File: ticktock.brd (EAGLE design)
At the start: 61 x 67.3 mm, 66 parts, among them IC1 ATMEGA644A, IC2 AD8611RM, IC3 REF200U, J1 AVR_SPI_PRG_6NS, Q1 MOSFET-NCHANNEL2N7002PW, Q2 MOSFET-NCHANNELBSS138, Q3 MOSFET-NCHANNELBSS138, U1 MAX232SOIC16, U2 OSCILLATORSMD, U3 FT232RLSSOP, U4 BMP180, X2 DB9 Male

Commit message: Relabel USB_TX and USB_RX to be consistent with MCU's perspective
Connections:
- net USB_RX: now also IC1.9, U3.1; no longer IC1.10, U3.5
- net USB_TX: now also IC1.10, U3.5; no longer IC1.9, U3.1
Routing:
- net USB_TX: track 27.5 -> 17.5 mm
- net USB_RX: track 17.5 -> 27.5 mm
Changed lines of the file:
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@@
 <wire x1="42.418" y1="8.108" x2="43.2" y2="8.89" width="0.381" layer="16"/>
 </signal>
-<signal name="USB_RX">
+<signal name="USB_TX">
 <contactref element="IC1" pad="10"/>
 <via x="30.734" y="6.858" extent="1-16" drill="0.6"/>
@@
 <wire x1="32.105" y1="7.721" x2="32.105" y2="8.736" width="0.4064" layer="1"/>
 </signal>
-<signal name="USB_TX">
+<signal name="USB_RX">
 <contactref element="IC1" pad="9"/>
 <via x="30.734" y="4.572" extent="1-16" drill="0.6"/>

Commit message: Reroute right angle wire
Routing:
- net MOSI: track 9.90 -> 11.0 mm
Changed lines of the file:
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@@
 <wire x1="30.48" y1="35.56" x2="31.242" y2="35.56" width="0.508" layer="1"/>
 <wire x1="31.242" y1="35.56" x2="32.258" y2="34.544" width="0.508" layer="1"/>
-<wire x1="32.258" y1="34.544" x2="32.258" y2="26.902" width="0.508" layer="1"/>
 <wire x1="32.258" y1="26.902" x2="32.3" y2="26.86" width="0.508" layer="1"/>
+<wire x1="32.258" y1="26.902" x2="31.772" y2="26.902" width="0.508" layer="1"/>
+<wire x1="31.772" y1="26.902" x2="31.242" y2="27.432" width="0.508" layer="1"/>
+<wire x1="31.242" y1="27.432" x2="31.242" y2="27.94" width="0.508" layer="1"/>
+<wire x1="31.242" y1="27.94" x2="32.258" y2="28.956" width="0.508" layer="1"/>
+<wire x1="32.258" y1="28.956" x2="32.258" y2="34.544" width="0.508" layer="1"/>
 </signal>
 <signal name="SCK">

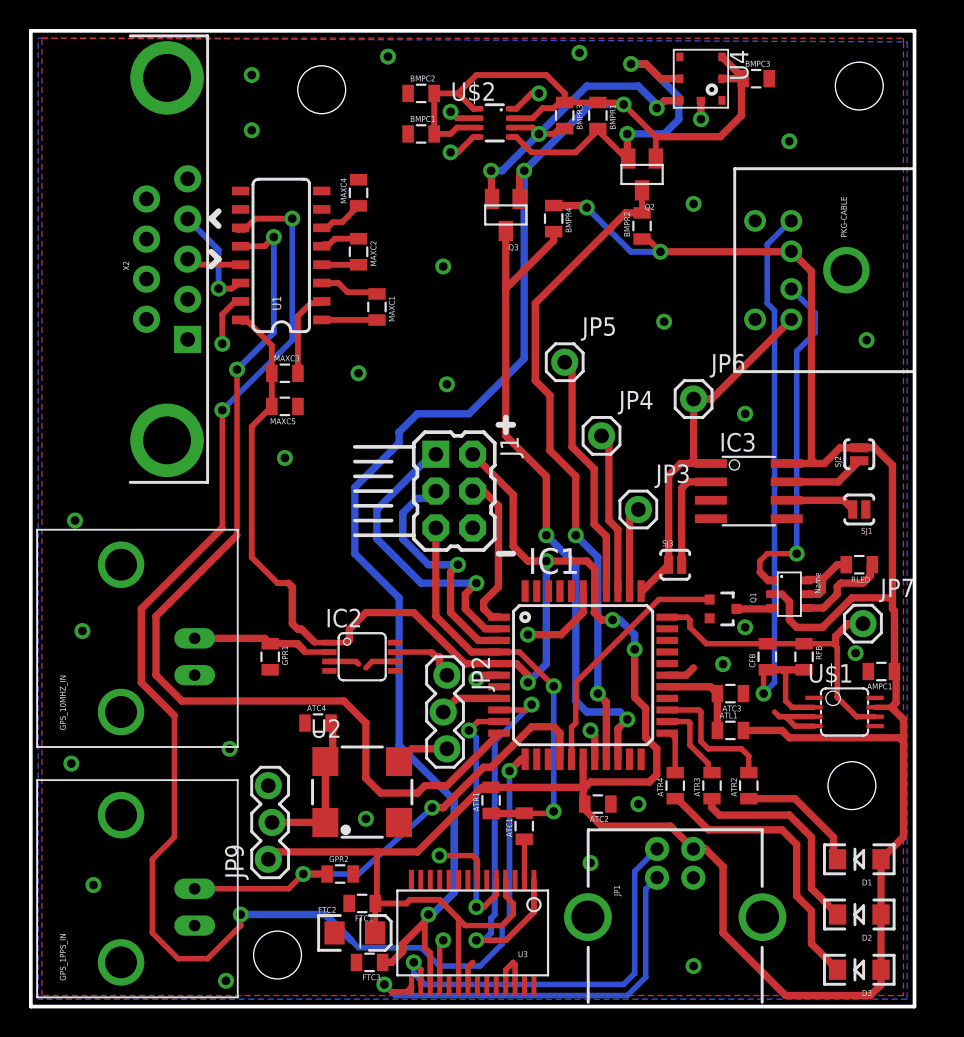
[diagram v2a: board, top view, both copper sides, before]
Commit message: Add silkscreen for MAX232
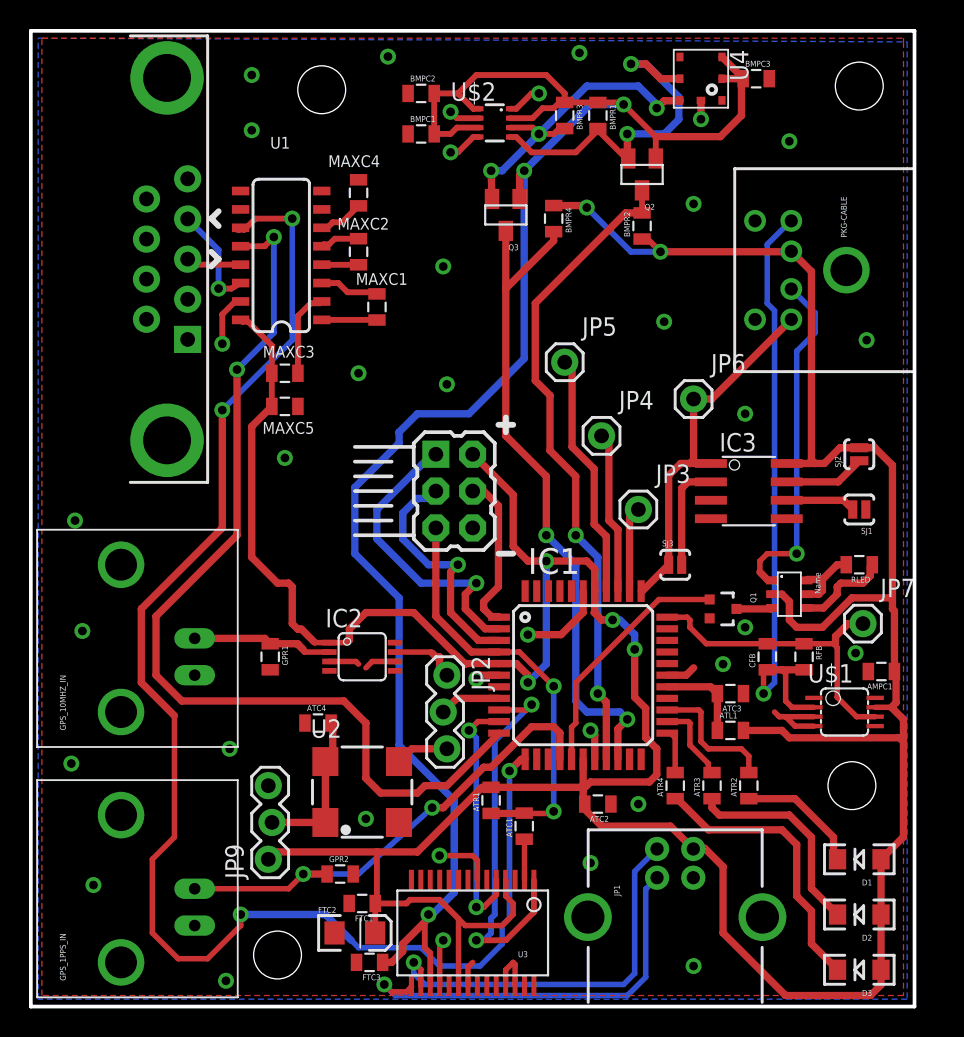
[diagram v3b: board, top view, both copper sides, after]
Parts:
- J1: value AVR_SPI_PRG_6NS -> ISP PGMR
- U1: value MAX232SOIC16 -> MAX232

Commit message: Start working on silkscreen
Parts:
- D1: value RED -> ERR
- D2: value Yellow -> ACT
- D3: value GREEN -> SEND
- GPS10MHZ, GPS1PPS: value BNCPTH -> BNC Conn
- IC2: value AD8611RM -> AD8611
- JP1: value USB-B -> Square USB
- U$2: value BME280BME280-LGA -> BME280
- U2: value OSCILLATORSMD -> 10MHz XTAL
- U3: value FT232RLSSOP -> FT232
- renumbered GPS_10MHZ_IN to GPS10MHZ, GPS_1PPS_IN to GPS1PPS
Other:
- board text added: "FTDI"
- board text added: "GPS"
- board text added: "MCU"
- board text added: "RS232"
- board text added: "SENSOR BLOCK"

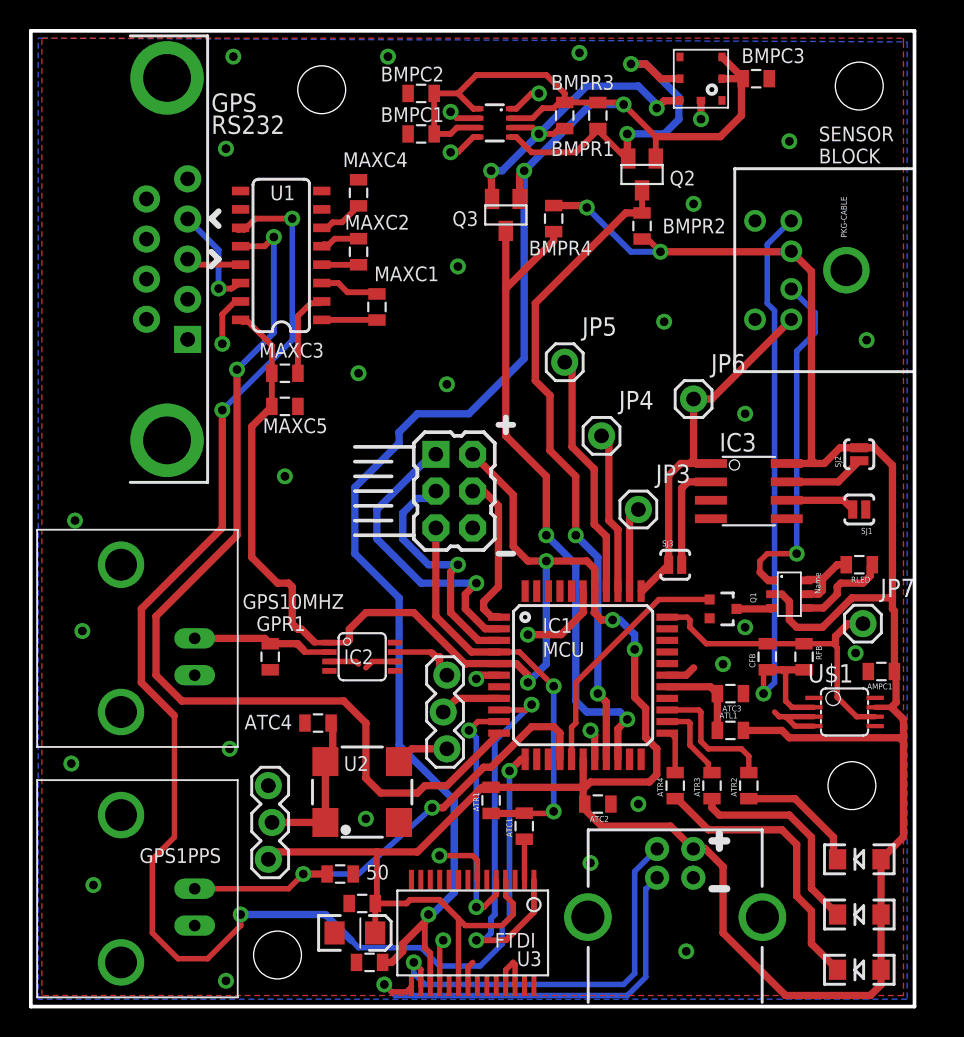
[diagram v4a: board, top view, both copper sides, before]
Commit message: Finish preliminary silkscreen
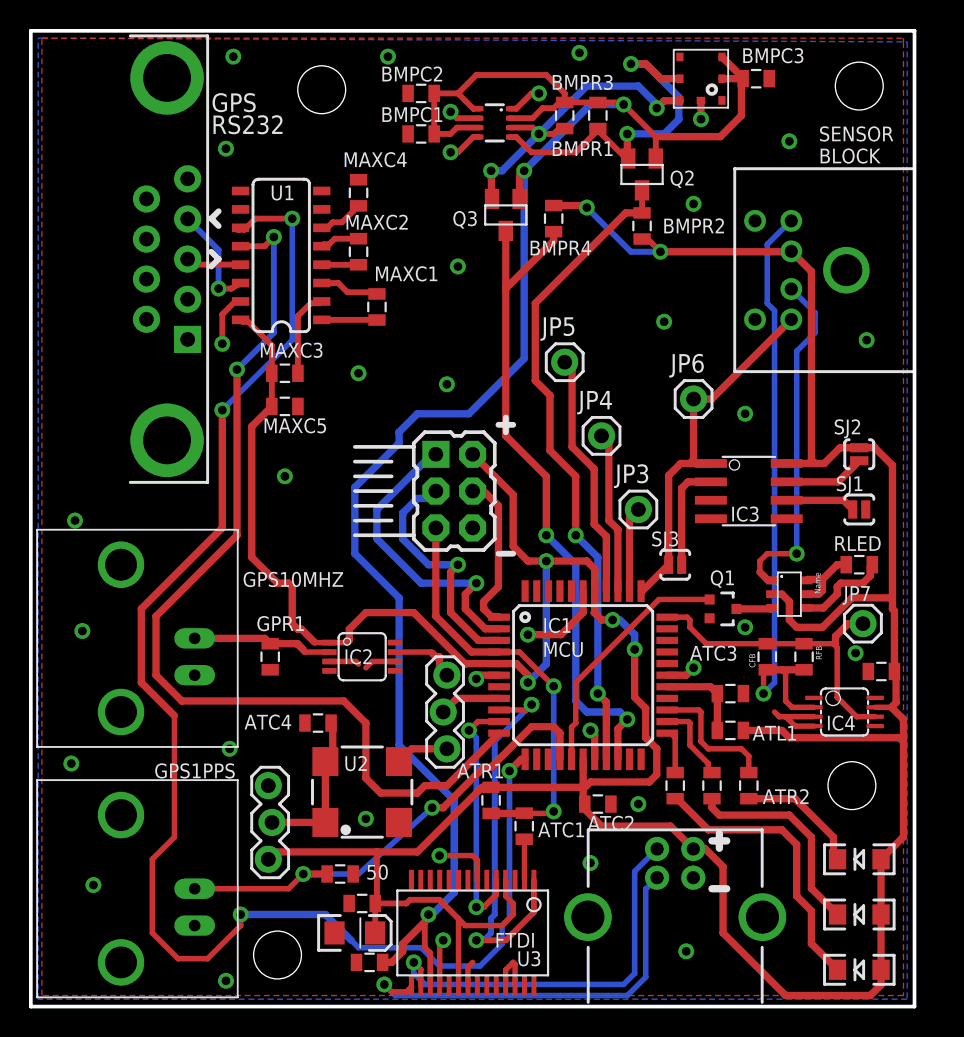
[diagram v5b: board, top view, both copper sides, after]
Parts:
- ATC1, ATC2: value 0.1uF -> .1uF
- IC3: value REF200U -> REF200
- PKG-CABLE: value MINI-DIN6PTH -> MINI DIN-6
- renumbered U$1 to IC4

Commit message: More work on silkscreen
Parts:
- U2: value 10MHz XTAL -> XTAL
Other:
- board text added: "CLK SEL"
- board text added: "PWR XTAL"
- board text added: "XTAL"
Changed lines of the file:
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@@
 <layer number="18" name="Vias" color="2" fill="1" visible="no" active="yes"/>
 <layer number="19" name="Unrouted" color="6" fill="1" visible="no" active="yes"/>
-<layer number="20" name="Dimension" color="15" fill="1" visible="no" active="yes"/>
-<layer number="21" name="tPlace" color="7" fill="1" visible="yes" active="yes"/>
+<layer number="20" name="Dimension" color="15" fill="1" visible="yes" active="yes"/>
+<layer number="21" name="tPlace" color="7" fill="1" visible="no" active="yes"/>
 <layer number="22" name="bPlace" color="7" fill="1" visible="no" active="yes"/>
-<layer number="23" name="tOrigins" color="15" fill="1" visible="yes" active="yes"/>
+<layer number="23" name="tOrigins" color="15" fill="1" visible="no" active="yes"/>
 <layer number="24" name="bOrigins" color="15" fill="1" visible="no" active="yes"/>
 <layer number="25" name="tNames" color="7" fill="1" visible="yes" active="yes"/>
@@
 <text x="54.356" y="58.166" size="1.016" layer="25" ratio="20">SENSOR
 BLOCK</text>
+<wire x1="18.288" y1="13.208" x2="18.288" y2="9.652" width="0.254" layer="25"/>
+<text x="19.05" y="9.652" size="0.508" layer="25" ratio="20" rot="R90">PWR XTAL</text>
+<wire x1="26.924" y1="20.828" x2="26.924" y2="17.272" width="0.254" layer="25"/>
+<wire x1="30.226" y1="19.812" x2="30.226" y2="23.368" width="0.254" layer="25"/>
+<text x="26.416" y="18.542" size="0.508" layer="25" ratio="20" rot="R90">XTAL</text>
+<text x="30.988" y="20.574" size="0.508" layer="25" ratio="20" rot="R90">GPS</text>
+<text x="27.178" y="24.892" size="1.016" layer="25" ratio="20">CLK
+SEL</text>
 </plain>
 <attributes>
@@
 </element>
 <element name="MAXC1" library="SparkFun-Capacitors" package="0805" value="1uF" x="23.876" y="48.26" smashed="yes" rot="R270">
-<attribute name="NAME" x="23.6855" y="50.038" size="1.016" layer="25" ratio="20"/>
 <attribute name="VALUE" x="25.019" y="48.768" size="1.016" layer="27" ratio="20"/>
 </element>
 <element name="MAXC2" library="SparkFun-Capacitors" package="0805" value="1uF" x="22.606" y="52.07" smashed="yes" rot="R270">
-<attribute name="NAME" x="21.6535" y="53.594" size="1.016" layer="25" ratio="20"/>
 <attribute name="VALUE" x="23.749" y="52.324" size="1.016" layer="27" ratio="20"/>
 </element>
@@
 </element>
 <element name="MAXC3" library="SparkFun-Capacitors" package="0805" value="1uF" x="17.526" y="43.688" smashed="yes">
-<attribute name="NAME" x="15.748" y="44.7675" size="1.016" layer="25" ratio="20"/>
 <attribute name="VALUE" x="19.304" y="43.561" size="1.016" layer="27" ratio="20"/>
 </element>
 <element name="MAXC5" library="SparkFun-Capacitors" package="0805" value="1uF" x="17.526" y="41.402" smashed="yes" rot="R180">
-<attribute name="NAME" x="16.002" y="39.5605" size="1.016" layer="25" ratio="20"/>
-<attribute name="VALUE" x="16.764" y="38.227" size="1.016" layer="27" ratio="20"/>
+<attribute name="VALUE" x="19.304" y="40.767" size="1.016" layer="27" ratio="20"/>
 </element>
 <element name="MAXC4" library="SparkFun-Capacitors" package="0805" value="1uF" x="22.606" y="56.134" smashed="yes" rot="R90">
-<attribute name="NAME" x="21.5265" y="57.912" size="1.016" layer="25" ratio="20"/>
 <attribute name="VALUE" x="23.749" y="56.642" size="1.016" layer="27" ratio="20"/>
 </element>
@@
 <attribute name="OC_FARNELL" value="1455123" x="38.1" y="22.86" size="1.778" layer="27" display="off"/>
 <attribute name="NAME" x="35.306" y="25.781" size="1.016" layer="25" ratio="20"/>
-<attribute name="VALUE" x="33.655" y="15.1209" size="1.016" layer="27" ratio="20"/>
 </element>
 <element name="U3" library="SparkFun-DigitalIC" package="SSOP28DB" value="FT232" x="30.48" y="5.08" smashed="yes" rot="R180">
@@
 </element>
 <element name="FTC1" library="SparkFun-Capacitors" package="0805" value="0.1uF" x="22.86" y="7.112" smashed="yes" rot="R180">
-<attribute name="VALUE" x="17.272" y="6.985" size="1.016" layer="27" ratio="20"/>
+<attribute name="VALUE" x="17.272" y="6.731" size="1.016" layer="27" ratio="20"/>
 </element>
 <element name="FTC3" library="SparkFun-Capacitors" package="0805" value="0.1uF" x="23.368" y="3.048" smashed="yes" rot="R180">
@@
 </element>
 <element name="ATC1" library="SparkFun-Capacitors" package="0805" value=".1uF" x="34.036" y="12.446" smashed="yes" rot="R90">
-<attribute name="NAME" x="34.9885" y="11.684" size="1.016" layer="25" ratio="20"/>
-<attribute name="VALUE" x="34.925" y="10.414" size="1.016" layer="27" ratio="20"/>
+<attribute name="VALUE" x="34.925" y="11.176" size="1.016" layer="27" ratio="20"/>
 </element>
 <element name="FTC2" library="SparkFun-Capacitors" package="EIA3216" value="10uF" x="22.352" y="5.08" smashed="yes">
-<attribute name="VALUE" x="16.156" y="5.65" size="1.016" layer="27" ratio="20"/>
+<attribute name="VALUE" x="16.156" y="5.396" size="1.016" layer="27" ratio="20"/>
 </element>
 <element name="ATR1" library="SparkFun-Resistors" package="0805" value="10K" x="31.75" y="14.224" smashed="yes" rot="R90">
-<attribute name="NAME" x="29.4005" y="15.748" size="1.016" layer="25" ratio="20"/>
 <attribute name="VALUE" x="28.321" y="14.478" size="1.016" layer="27" ratio="20"/>
 </element>
 <element name="ATC2" library="SparkFun-Capacitors" package="0805" value=".1uF" x="39.116" y="13.97" smashed="yes" rot="R180">
-<attribute name="NAME" x="38.4048" y="12.1285" size="1.016" layer="25" ratio="20"/>
 <attribute name="VALUE" x="40.64" y="13.843" size="1.016" layer="27" ratio="20"/>
 </element>
 <element name="ATL1" library="SparkFun-Passives" package="0805" value="10uH" x="48.26" y="19.05" smashed="yes">
-<attribute name="NAME" x="49.784" y="18.3515" size="1.016" layer="25" ratio="20"/>
-<attribute name="VALUE" x="49.022" y="17.145" size="1.016" layer="27" ratio="20"/>
+<attribute name="VALUE" x="49.53" y="17.399" size="1.016" layer="27" ratio="20"/>
 </element>
 <element name="ATC3" library="SparkFun-Capacitors" package="0805" value="0.1uF" x="48.26" y="21.59" smashed="yes" rot="R180">
-<attribute name="NAME" x="45.466" y="23.8633" size="1.016" layer="25" ratio="20"/>
 <attribute name="VALUE" x="45.466" y="22.733" size="1.016" layer="27" ratio="20"/>
 </element>
@@
 <attribute name="VALUE" x="22.987" y="40.132" size="1.016" layer="27" ratio="20"/>
 </element>
-<element name="U2" library="SparkFun-FreqCtrl" package="CRYSTAL-SMD-7X5" value="10MHz XTAL" x="20.32" y="12.7" smashed="yes">
+<element name="U2" library="SparkFun-FreqCtrl" package="CRYSTAL-SMD-7X5" value="XTAL" x="20.32" y="12.7" smashed="yes">
 <attribute name="NAME" x="21.59" y="16.256" size="1.016" layer="25" ratio="20"/>
-<attribute name="VALUE" x="18.288" y="10.287" size="1.016" layer="27" ratio="20"/>
+<attribute name="VALUE" x="23.368" y="10.287" size="1.016" layer="27" ratio="20"/>
 </element>
 <element name="ATC4" library="SparkFun-Capacitors" package="0805" value="0.01uF" x="19.812" y="19.558" smashed="yes">
@@
 </element>
 <element name="GPR1" library="SparkFun-Resistors" package="0805" value="50" x="16.51" y="24.13" smashed="yes" rot="R270">
-<attribute name="NAME" x="15.5575" y="25.908" size="1.016" layer="25" ratio="20"/>
-<attribute name="VALUE" x="17.399" y="24.638" size="1.016" layer="27" ratio="20"/>
+<attribute name="VALUE" x="15.621" y="25.908" size="1.016" layer="27" ratio="20"/>
 </element>
 <element name="GPR2" library="SparkFun-Resistors" package="0805" value="50" x="21.336" y="9.144" smashed="yes">
-<attribute name="VALUE" x="23.114" y="8.763" size="1.016" layer="25" ratio="20"/>
+<attribute name="VALUE" x="22.86" y="8.763" size="1.016" layer="25" ratio="20"/>
 </element>
 <element name="RFB" library="SparkFun-Resistors" package="0805" value="1K" x="53.34" y="24.13" smashed="yes" rot="R270">
@@
 </element>
 <element name="BMPR1" library="SparkFun-Resistors" package="0805" value="10K" x="39.116" y="61.468" smashed="yes" rot="R270">
-<attribute name="NAME" x="35.8775" y="58.674" size="1.016" layer="25" ratio="20"/>
+<attribute name="VALUE" x="37.211" y="58.674" size="1.016" layer="27" ratio="20"/>
 </element>
 <element name="BMPR2" library="SparkFun-Resistors" package="0805" value="10K" x="42.164" y="53.848" smashed="yes" rot="R90">
@@
 </element>
 <element name="BMPR3" library="SparkFun-Resistors" package="0805" value="10K" x="36.83" y="61.468" smashed="yes" rot="R270">
-<attribute name="NAME" x="35.8775" y="63.246" size="1.016" layer="25" ratio="20"/>
-<attribute name="VALUE" x="34.417" y="64.516" size="1.016" layer="27" ratio="20"/>
+<attribute name="NAME" x="35.8775" y="64.516" size="1.016" layer="25" ratio="20"/>
+<attribute name="VALUE" x="35.941" y="63.246" size="1.016" layer="27" ratio="20"/>
 </element>
 <element name="BMPR4" library="SparkFun-Resistors" package="0805" value="10K" x="36.068" y="54.356" smashed="yes" rot="R270">
@@
 </element>
 <element name="BMPC1" library="SparkFun-Capacitors" package="0805" value="100nF" x="26.924" y="60.198" smashed="yes">
-<attribute name="NAME" x="24.13" y="61.0235" size="1.016" layer="25" ratio="20"/>
+<attribute name="VALUE" x="20.828" y="59.563" size="1.016" layer="27" ratio="20"/>
 </element>
 <element name="ATR2" library="SparkFun-Resistors" package="0805" value="330" x="49.53" y="15.24" smashed="yes" rot="R90">
@@
 </element>
 <element name="BMPC2" library="SparkFun-Capacitors" package="0805" value="100nF" x="26.924" y="62.992" smashed="yes">
-<attribute name="NAME" x="24.13" y="63.8175" size="1.016" layer="25" ratio="20"/>
-<attribute name="VALUE" x="25.654" y="65.151" size="1.016" layer="27" ratio="20"/>
+<attribute name="NAME" x="23.876" y="65.0875" size="1.016" layer="25" ratio="20"/>
+<attribute name="VALUE" x="25.4" y="63.881" size="1.016" layer="27" ratio="20"/>
 </element>
 <element name="U4" library="SparkFun-Sensors" package="BMP180" value="BMP180" x="46.228" y="64.008" smashed="yes" rot="R270">
